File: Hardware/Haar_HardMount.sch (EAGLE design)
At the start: 17 parts, among them J1 SOLDERCUP_CONN_QUAD, Q1 2N7002, U1 SHT35DFN, U2 LPS35HW, U4 TPS62237DRY, U5 TXS0102DQM

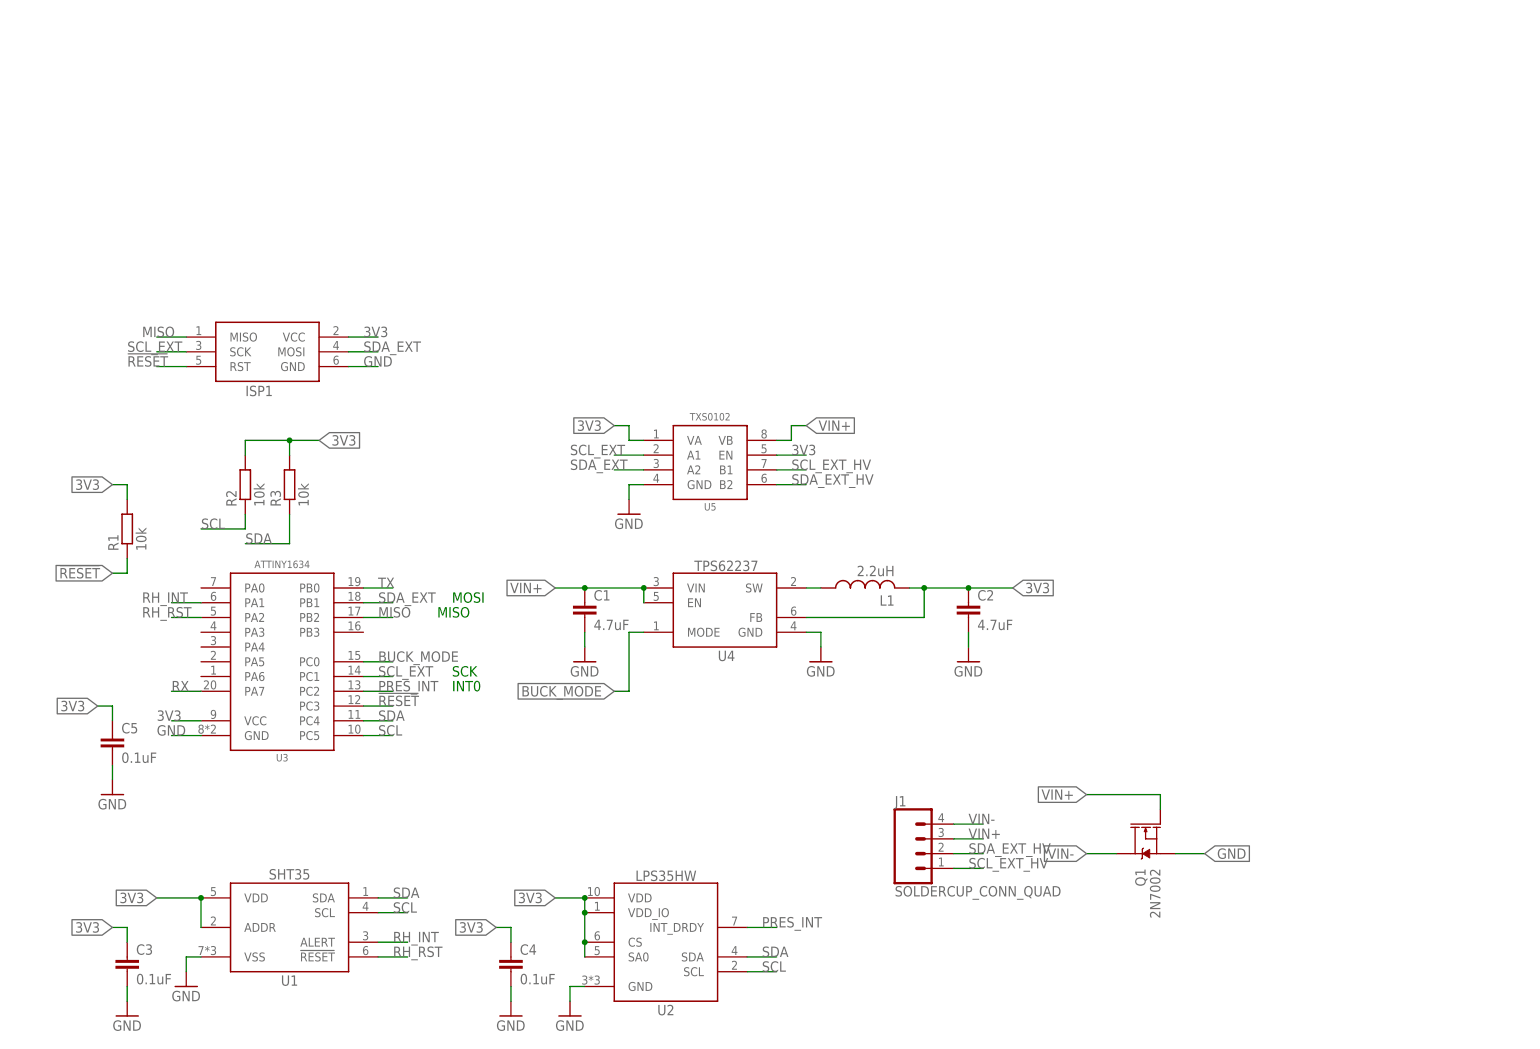
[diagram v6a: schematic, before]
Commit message: Adjusted folders, added production documents
Added BoM, added frame to Eagle schematic, moved production files into own folder, renamed folder to `Software`, and moved old design to `legacy` folder.
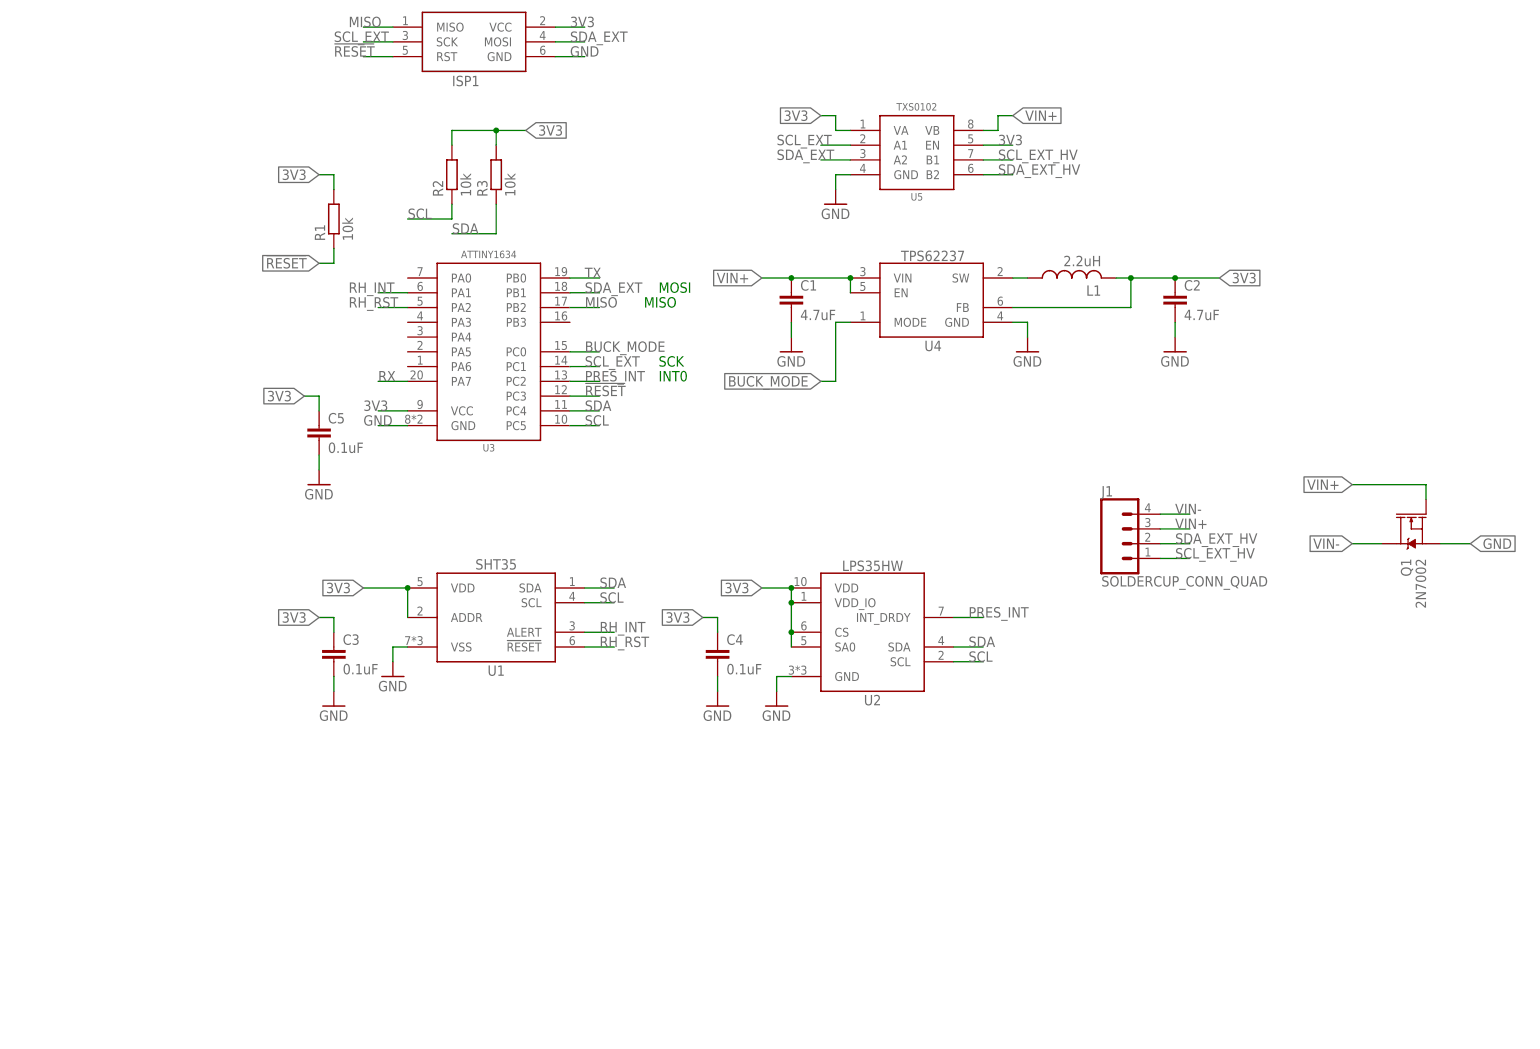
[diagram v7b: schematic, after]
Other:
- moved on the sheet: C1, C2, C3, C4, C5, ISP1, J1, L1, Q1, R1, R2, R3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
